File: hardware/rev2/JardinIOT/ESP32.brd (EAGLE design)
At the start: 160 x 100 mm, 32 parts, among them IC1 7815TV, IC2 7812TV, Q1 BD243, Q2 BD243, Q3 BD243, Q4 BD243

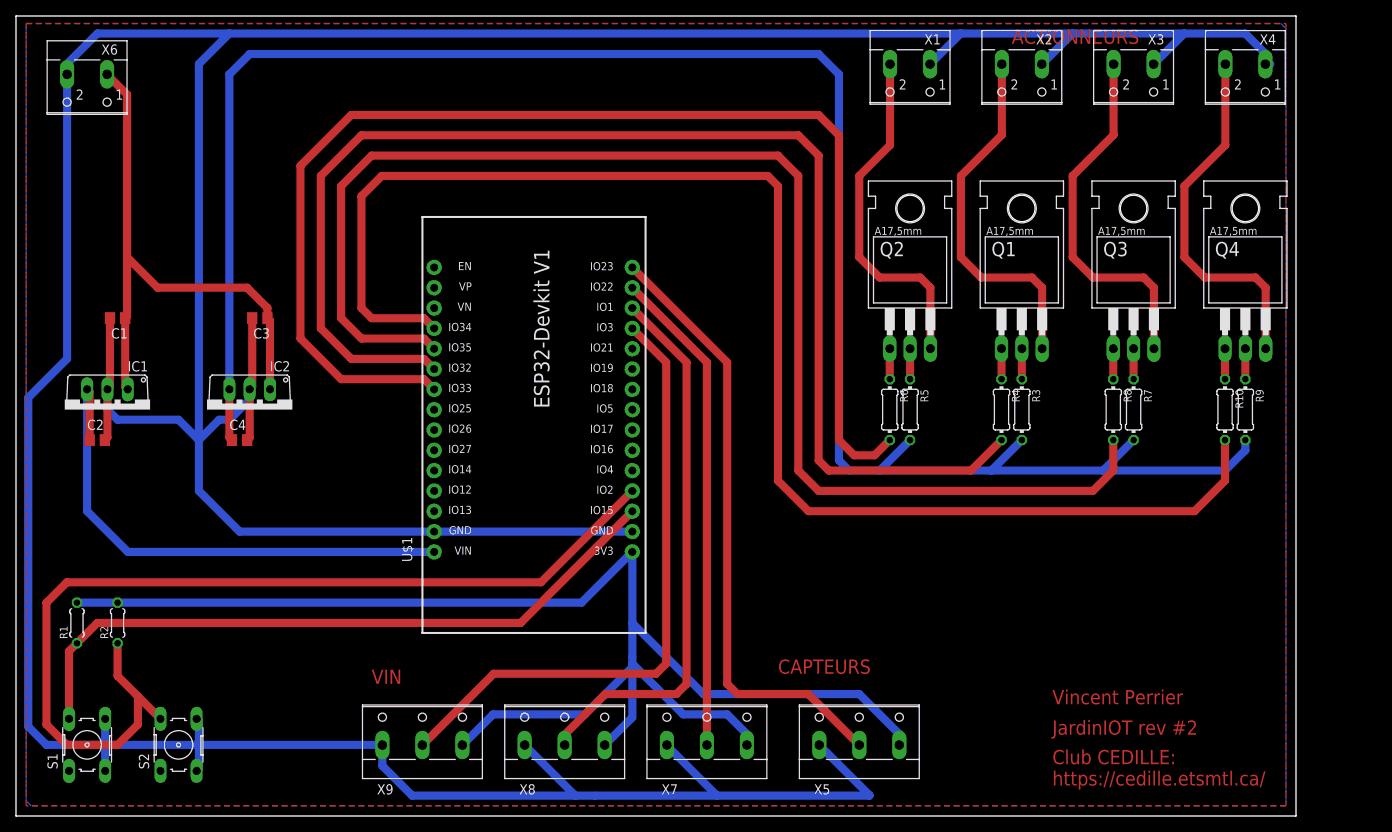
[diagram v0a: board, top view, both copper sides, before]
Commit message: Meilleur mappage des broches du ESP32 sur le PCB
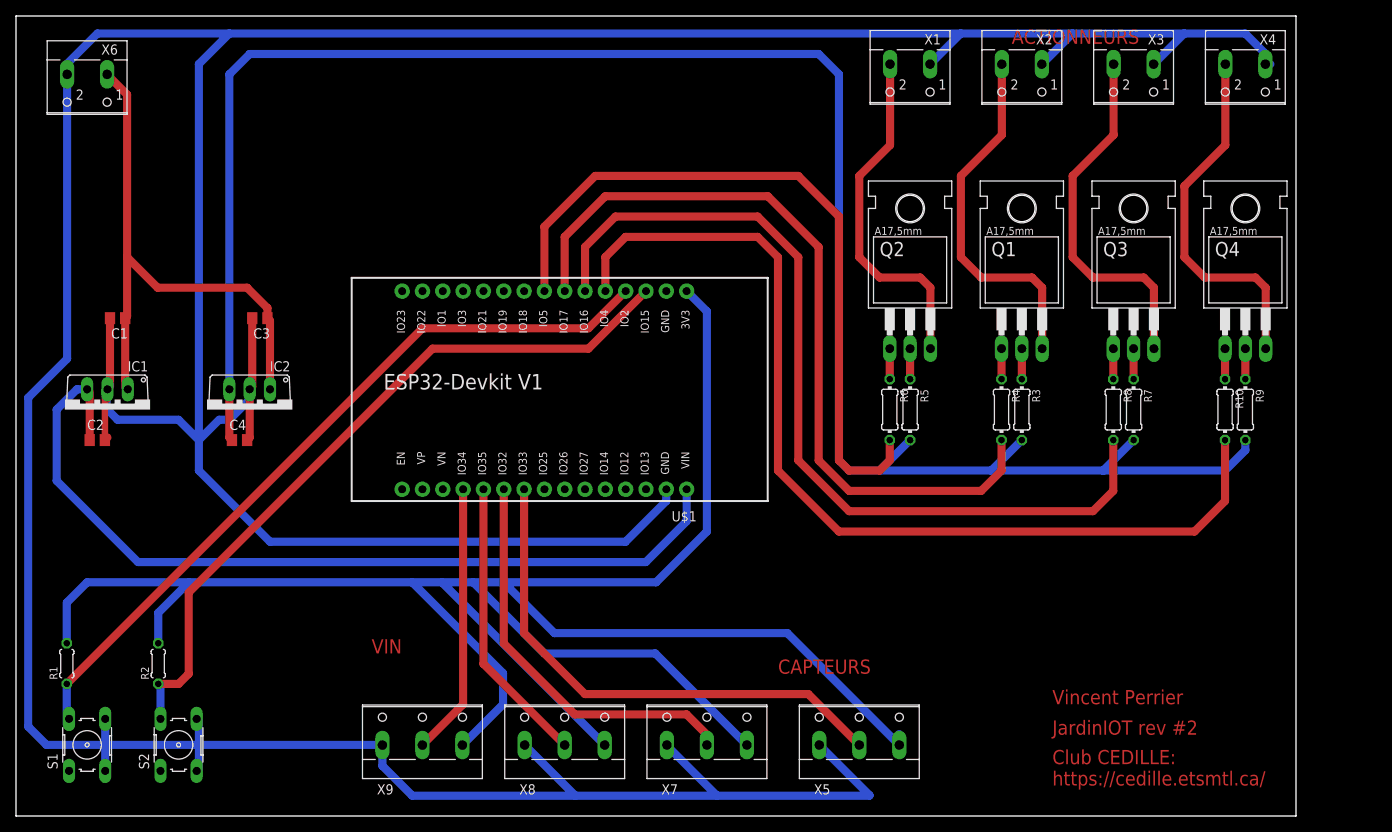
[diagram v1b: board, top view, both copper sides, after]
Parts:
- IC1: value 7815TV -> 7805TV
- moved R2 7.18 mm to (17.8, 19.1)
- moved R1 5.24 mm to (6.35, 19.1)
- moved U$1 4.58 mm to (61.0, 52.1), turned to 180 degrees
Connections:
- net N$1: now also U$1.4; no longer U$1.3
- net N$15: now also R4.2, U$1.7; no longer R10.2, U$1.19
- net N$16: now also U$1.22; no longer U$1.15
- net N$17: now also U$1.6; no longer U$1.20
- net N$18: now also U$1.8; no longer U$1.22
- net N$19: now also R10.2, U$1.5; no longer R4.2, U$1.21
- net N$20: now also U$1.21; no longer U$1.14
- net N$21: now also U$1.20; no longer U$1.13
- net N$22: now also U$1.19; no longer U$1.12
- net N$3: now also U$1.3; no longer U$1.4
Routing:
- net 3V3: track 182.7 -> 288.1 mm
- net N$15: track 178.7 -> 99.2 mm
- net N$18: track 158.0 -> 90.0 mm
- net N$17: track 171.6 -> 110.7 mm
- net N$22: track 78.4 -> 34.1 mm
- net 5V_VCC: track 67.2 -> 108.9 mm
- net N$19: track 163.8 -> 122.8 mm
- net N$21: track 68.9 -> 37.5 mm
- net N$3: track 123.0 -> 91.7 mm
- net N$16: track 76.6 -> 65.7 mm
- net N$20: track 61.0 -> 50.7 mm
- net N$1: track 86.1 -> 95.3 mm
- net GND: track 577.4 -> 585.4 mm
- net 20VDC: track 71.1 -> 72.2 mm
- removed copper zone on layer 16, net CPBOTTOM
- removed copper zone on layer 1, net CPTOP
